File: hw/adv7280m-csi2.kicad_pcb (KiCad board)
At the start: 4 copper layers, 42 x 32 mm, 50 parts, among them J1 RPi_CSI_15pin, J2 CVBS_RCA, J3 CVBS_SMA, U1 ADV7280WBCPZ-M, U2 AP2112K-1.8, U3 AP2112K-1.8, Y1 28.63636MHz

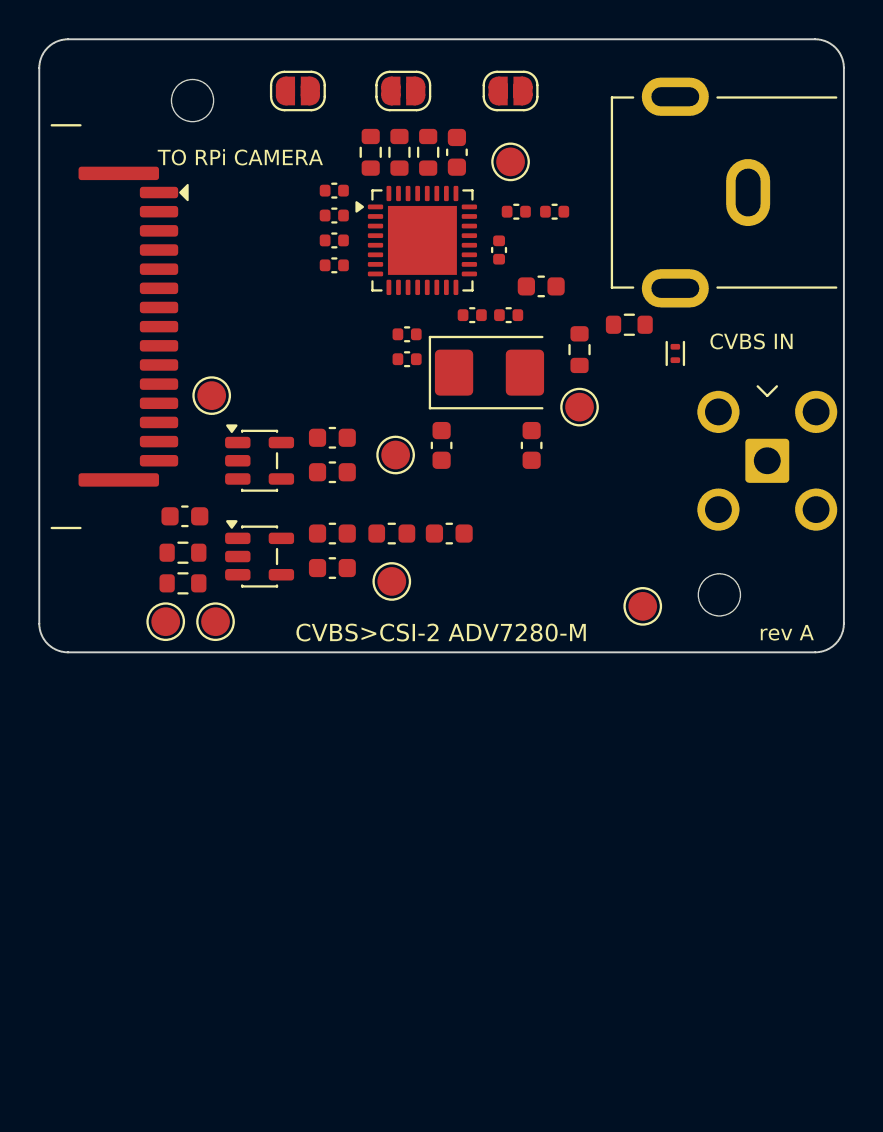
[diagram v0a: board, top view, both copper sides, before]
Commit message: Stage 3: routing (tools/route_pcb.py), zones, length-matched MIPI, DRC clean
- MIPI pairs 0.18/0.15 mm on F.Cu, one crossover via pair per lane
  (connector pin order is inverted vs. the chip), skew <= 0.04 mm
- In1 solid GND, In2 power polygons, PVDD on B.Cu, GND pours top/bottom
- thermal-pad via array, per-pad GND vias, I2C/CAM_GPIO on B.Cu
- project rules/netclasses written by tools/write_pro.py
- DRC with schematic parity: 0 errors, 0 warnings, 0 unconnected
- docs: renders, per-layer images, assumptions stage 3

Co-Authored-By: Claude Fable 5.1 <noreply@anthropic.com>
Claude-Session: https://claude.ai/code/session_017Xy941kmWX9XJsHmZMcZcK
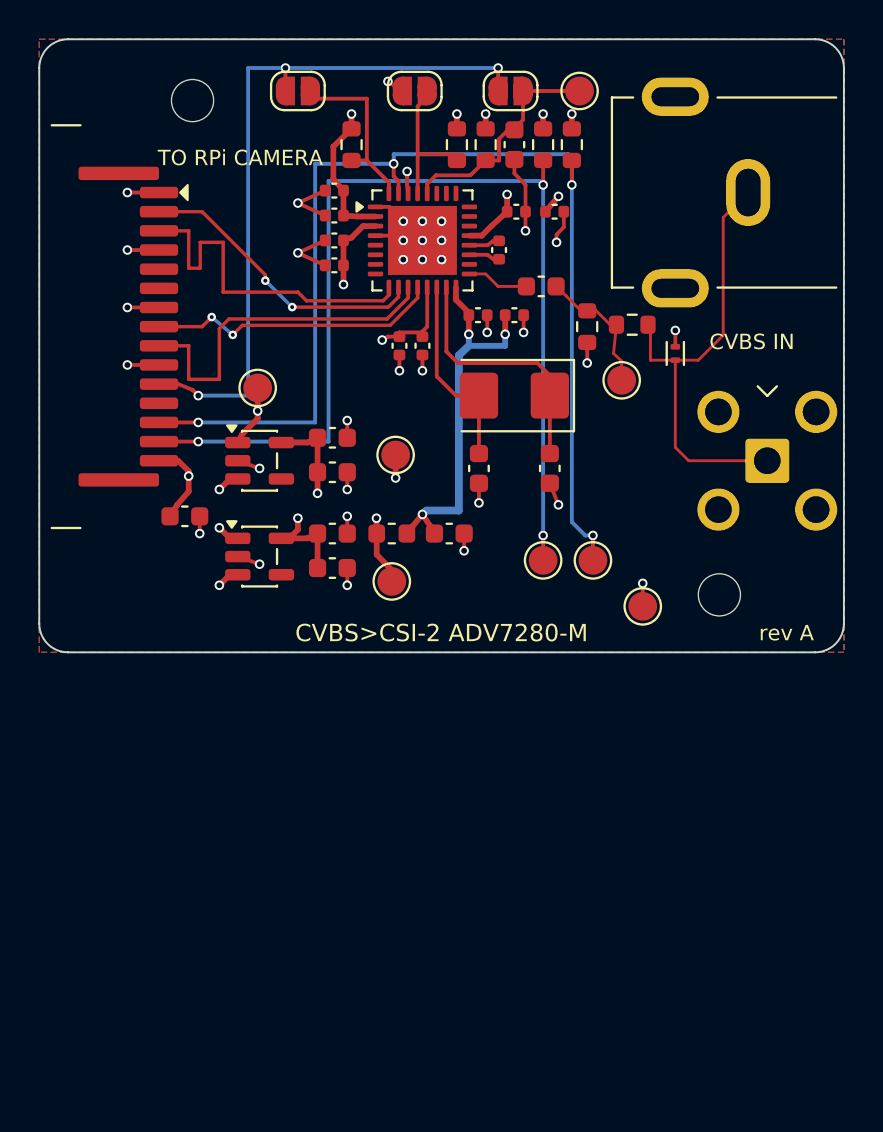
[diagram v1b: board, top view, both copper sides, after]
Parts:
- moved R7 30.6 mm to (27.8, 5.50), turned to -90 degrees
- moved R6 28.4 mm to (26.3, 5.50), turned to -90 degrees
- moved TP3 20.0 mm to (26.3, 27.2)
- moved TP4 20.0 mm to (28.9, 27.2)
- moved TP5 5.16 mm to (28.2, 2.70)
- moved C5 3.03 mm to (24.8, 5.50), turned to -90 degrees
- moved R3 3.03 mm to (23.3, 5.50), turned to -90 degrees
- moved R5 3.03 mm to (21.8, 5.50), turned to -90 degrees
- moved TP7 2.61 mm to (30.4, 17.8)
- moved TP1 2.43 mm to (11.4, 18.2)
- moved C2 2.29 mm to (22.9, 22.4)
- moved Y1 1.77 mm to (24.8, 18.6), turned to 180 degrees
- moved C3 1.53 mm to (26.6, 22.4)
- moved R2 1.26 mm to (28.6, 15.0), turned to -90 degrees
- moved R4 1.08 mm to (16.3, 5.50), turned to -90 degrees
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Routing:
- net /SCL: track 0.00 -> 60.3 mm, vias 0 -> 4
- net /SDA: track 0.00 -> 56.3 mm, vias 0 -> 4
- net GND: track 0.00 -> 37.6 mm, vias 0 -> 35
- net /CAM_GPIO: track 0.00 -> 37.4 mm, vias 0 -> 3
- net /CVBS_IN: track 0.00 -> 23.8 mm
- net +3V3: track 0.00 -> 21.9 mm, vias 0 -> 10
- net PVDD: track 0.00 -> 20.1 mm, vias 0 -> 3
- net /CSI_CLKP: track 0.00 -> 18.6 mm
- net /CSI_D0P: track 0.00 -> 18.6 mm
- net /CSI_D0N: track 0.00 -> 15.5 mm, vias 0 -> 2
- net /CSI_CLKN: track 0.00 -> 15.4 mm, vias 0 -> 2
- net +1V8D: track 0.00 -> 15.3 mm, vias 0 -> 4
- net +1V8A: track 0.00 -> 13.4 mm, vias 0 -> 4
- net Net-(U1-XTALN): track 0.00 -> 13.3 mm
- net /~{RESET}: track 0.00 -> 12.0 mm
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- added copper zone on In2.Cu, net +1V8A
- added copper zone on In2.Cu, net +1V8D
- added copper zone on In2.Cu, net +3V3
- added copper zone on B.Cu, net GND
- added copper zone on F.Cu, net GND
- added copper zone on In1.Cu, net GND

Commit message: Remove SMA input connector (J3): RCA only; regenerate schematic, board, docs
Co-Authored-By: Claude Fable 5.1 <noreply@anthropic.com>
Claude-Session: https://claude.ai/code/session_017Xy941kmWX9XJsHmZMcZcK
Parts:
- removed J3: CVBS_SMA, adv-parts:SMA_BWSMA-KWE-Z001_EdgeMount
- moved TP6 9.10 mm to (36.5, 22.0)
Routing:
- net /CVBS_IN: track 23.8 -> 14.2 mm

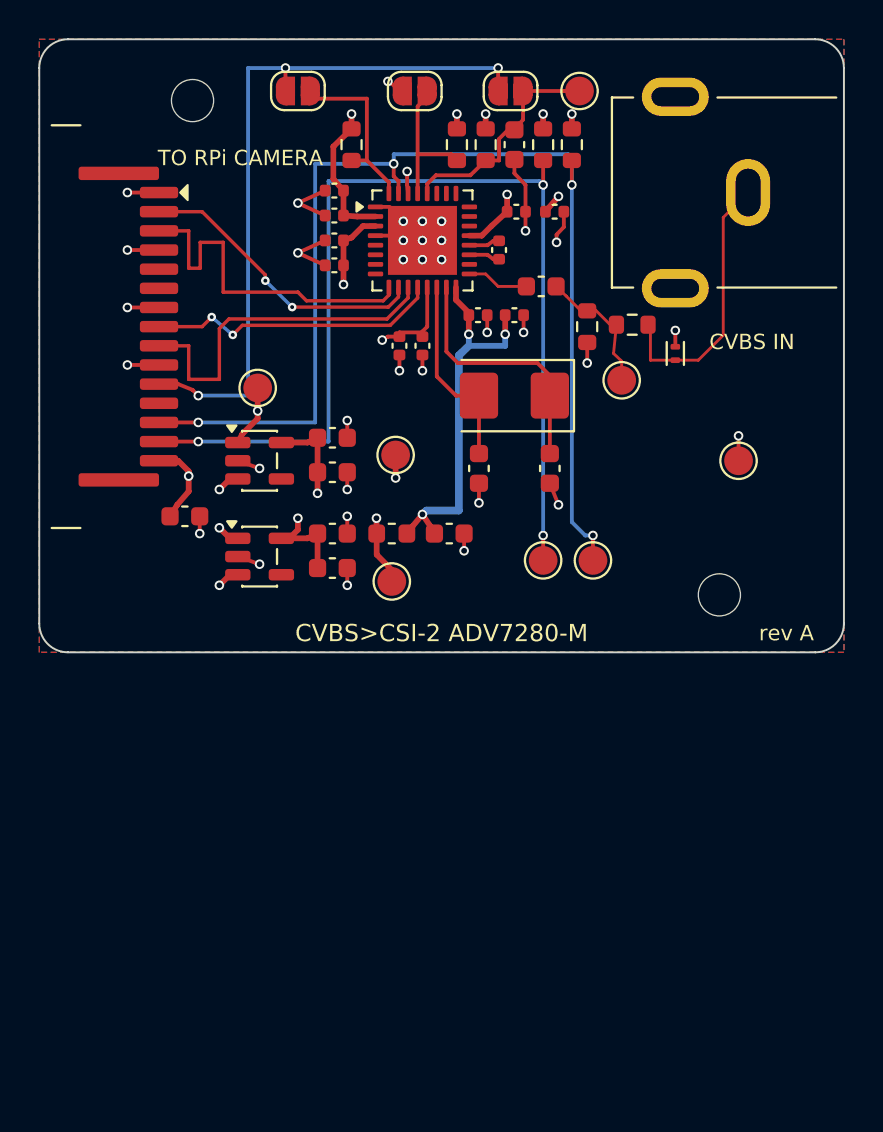
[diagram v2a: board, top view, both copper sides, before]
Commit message: Stage 5b: buffer section placement (42x55 board, breakaway slot with two tabs), RESET C5 4.7 uF, render script
- gen_pcb.py: outline with 2 mm slot and 2.5 mm tabs, placement of THS7314 section, silkscreen, rev B
- route_pcb.py: zones cover the whole outline
- C5 1 uF -> 4.7 uF (tau 47 ms, RESET low >= 13 ms); UG-637 figure reference fixed
- tools/render.sh regenerates docs/render-*.png and layer images
- assumptions A5-5 decided, A5-9 added; docs updated

Co-Authored-By: Claude Fable 5.1 <noreply@anthropic.com>
Claude-Session: https://claude.ai/code/session_017Xy941kmWX9XJsHmZMcZcK
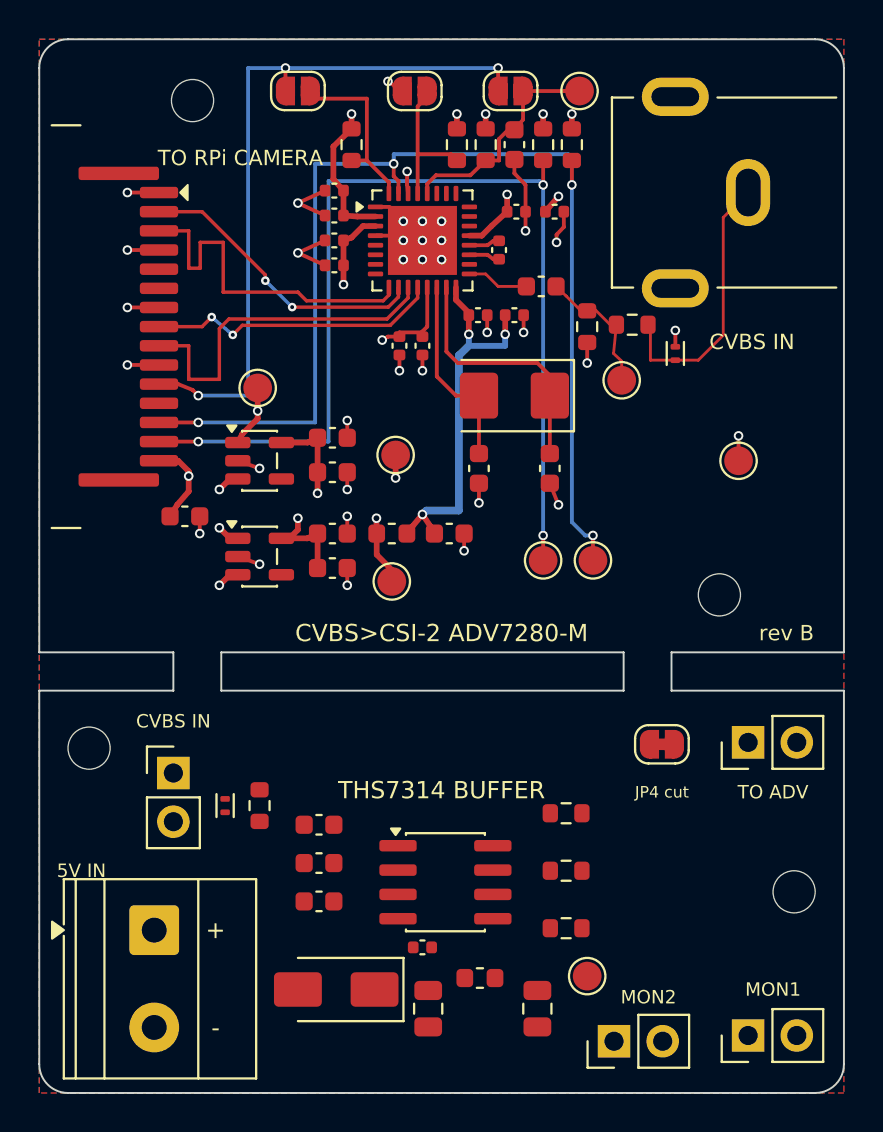
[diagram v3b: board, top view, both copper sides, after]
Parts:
- added C23: 100nF, Capacitor_SMD:C_0603_1608Metric, F.Cu at (14.6, 41.0)
- added C24: 100nF, Capacitor_SMD:C_0603_1608Metric, F.Cu at (14.6, 43.0)
- added C25: 100nF, Capacitor_SMD:C_0603_1608Metric, F.Cu at (14.6, 45.0)
- added C26: 100nF, Capacitor_SMD:C_0402_1005Metric, F.Cu at (20.0, 47.4)
- added C27: 10uF, Capacitor_SMD:C_0805_2012Metric, F.Cu at (26.0, 50.6)
- added C28: 22uF, Capacitor_SMD:C_0805_2012Metric, F.Cu at (20.3, 50.6)
- added D2: SS14, Diode_SMD:D_SMA, F.Cu at (15.5, 49.6)
- added D3: TPD1E10B06, adv-parts:TI_X1SON-2_DPY0002A_1.0x0.6mm, F.Cu at (9.70, 40.0)
- added FB2: 120R@100MHz, Inductor_SMD:L_0603_1608Metric, F.Cu at (23.0, 49.0)
- added H3: M2, MountingHole:MountingHole_2.2mm_M2, F.Cu at (2.60, 37.0)
- added H4: M2, MountingHole:MountingHole_2.2mm_M2, F.Cu at (39.4, 44.5)
- added J4: 5V_IN, TerminalBlock_Phoenix:TerminalBlock_Phoenix_MKDS-1,5-2-5.08_1x02_P5.08mm_Horizontal, F.Cu at (6.00, 46.5)
- added J5: CVBS_IN_HDR, Connector_PinHeader_2.54mm:PinHeader_1x02_P2.54mm_Vertical, F.Cu at (7.00, 38.3)
- added J6: MON1_HDR, Connector_PinHeader_2.54mm:PinHeader_1x02_P2.54mm_Vertical, F.Cu at (37.0, 52.0)
- added J7: MON2_HDR, Connector_PinHeader_2.54mm:PinHeader_1x02_P2.54mm_Vertical, F.Cu at (30.0, 52.3)
- added J8: CVBS_BUF_HDR, Connector_PinHeader_2.54mm:PinHeader_1x02_P2.54mm_Vertical, F.Cu at (37.0, 36.7)
- added JP4: BUF>ADV, Jumper:SolderJumper-2_P1.3mm_Bridged_RoundedPad1.0x1.5mm, F.Cu at (32.5, 36.8)
- added R10: 75, Resistor_SMD:R_0603_1608Metric, F.Cu at (27.5, 43.4)
- added R11: 75, Resistor_SMD:R_0603_1608Metric, F.Cu at (27.5, 46.4)
- added R8: 75, Resistor_SMD:R_0603_1608Metric, F.Cu at (11.5, 40.0)
- added R9: 75, Resistor_SMD:R_0603_1608Metric, F.Cu at (27.5, 40.4)
- added TP9: VS_BUF, TestPoint:TestPoint_Pad_D1.5mm, F.Cu at (28.6, 48.9)
- added U5: THS7314DR, Package_SO:SOIC-8_3.9x4.9mm_P1.27mm, F.Cu at (21.2, 44.0)
- C5: value 1uF -> 4.7uF
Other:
- board size 42 x 32 mm -> 42 x 55 mm
- board text added: "+"
- board text added: "-"
- board text added: "5V IN"
- board text added: "ADV7280M-CSI2 rev B github inestvan/adv"
- board text added: "JP4 cut"
- board text added: "MON1"
- board text added: "MON2"
- board text added: "THS7314 BUFFER"
- board text added: "THS7314 BUFFER rev B"
- board text added: "TO ADV"
- board text added: "rev B"
- board text removed: "ADV7280M-CSI2 rev A github inestvan/adv"
- board text removed: "rev A"

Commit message: Stage 5c: route THS7314 buffer section, CVBS_IN link through the tab, GND stitching; MIPI return-path fix; DRC clean
- route_pcb.py: buffer nets (input node, coupling caps, outputs, 5 V chain), 22 GND vias, In2 GND zone under the section
- +3V3 In2 zone extended under the D0N crossover stub, +1V8D notched; GND return vias next to the D0N vias
- DRC: 0 violations, 0 unconnected; renders and layer images regenerated
- assumptions A5-10, A5-11

Co-Authored-By: Claude Fable 5.1 <noreply@anthropic.com>
Claude-Session: https://claude.ai/code/session_017Xy941kmWX9XJsHmZMcZcK
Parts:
- turned C26 to 180 degrees
- turned D3 to -90 degrees
- turned R8 to -90 degrees
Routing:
- net /CVBS_IN: track 14.2 -> 34.3 mm
- net /CVBS_SRC: track 0.00 -> 17.6 mm
- net /VS_BUF: track 0.00 -> 16.9 mm
- net /MON1: track 0.00 -> 12.8 mm
- net /CVBS_BUF: track 0.00 -> 11.7 mm
- net /5V_IN: track 0.00 -> 8.78 mm
- net /5V_BUF: track 0.00 -> 8.74 mm
- net /MON2: track 0.00 -> 7.52 mm
- net GND: track 37.7 -> 43.8 mm, vias 35 -> 59
- net Net-(U5-CH1_IN): track 0.00 -> 3.80 mm
- net Net-(U5-CH3_OUT): track 0.00 -> 3.73 mm
- net Net-(U5-CH1_OUT): track 0.00 -> 3.70 mm
- net Net-(U5-CH3_IN): track 0.00 -> 3.50 mm
- net Net-(U5-CH2_IN): track 0.00 -> 3.50 mm
- net Net-(U5-CH2_OUT): track 0.00 -> 3.00 mm
- added copper zone on In2.Cu, net GND
